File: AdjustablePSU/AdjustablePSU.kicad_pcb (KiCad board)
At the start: 2 copper layers, 99.1 x 96.5 mm, 39 parts

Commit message: RevC update
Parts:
- added HS1: Heatsink, Heatsink:Heatsink_SheetType_50x7mm_2Fixations, F.Cu at (149.4, 59.8)
- C_NEG6, C_POS6: footprint Capacitor_SMD:CP_Elec_6.3x3.9 -> Capacitor_SMD:CP_Elec_10x12.6
- moved D_POS3 3.43 mm to (179.6, 76.7)
- moved D_POS2 3.08 mm to (173.1, 76.8)
- moved D_NEG3 2.30 mm to (116.1, 77.5)
- moved D_POS1 2.21 mm to (165.6, 76.8)
- moved D_NEG2 1.63 mm to (123.3, 77.5)
- moved D_NEG1 0.13 mm to (130.6, 77.5)
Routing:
- net GND: track 90.1 -> 93.9 mm
- net /DC_POS_IN: track 121.1 -> 118.1 mm
- net /AC_IN: track 76.6 -> 74.2 mm
- net /12VDC_POS_REG: track 97.5 -> 99.5 mm
- net /DC_NEG_IN: track 126.8 -> 125.1 mm
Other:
- board text added: "Rev C Chris Sutton 0619"

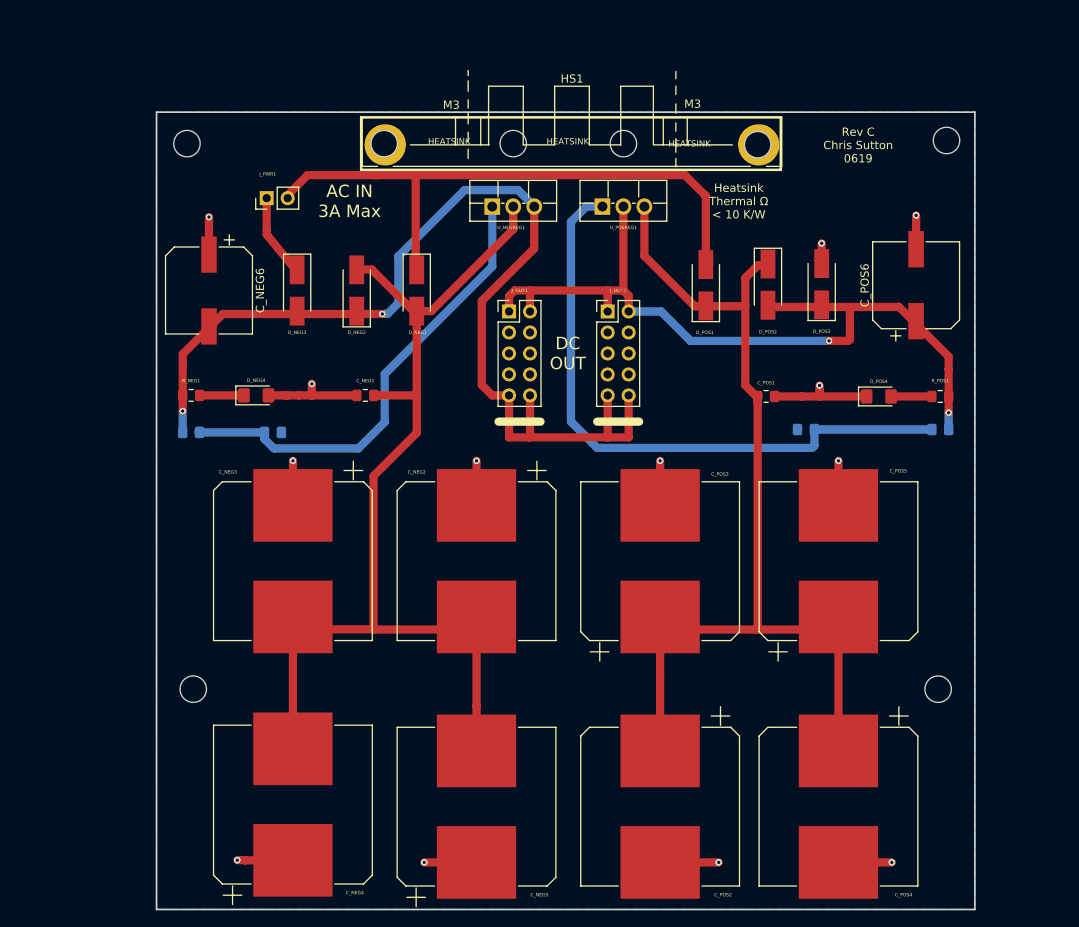
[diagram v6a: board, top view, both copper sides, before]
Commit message: Added hybrid THT/SMT RevD
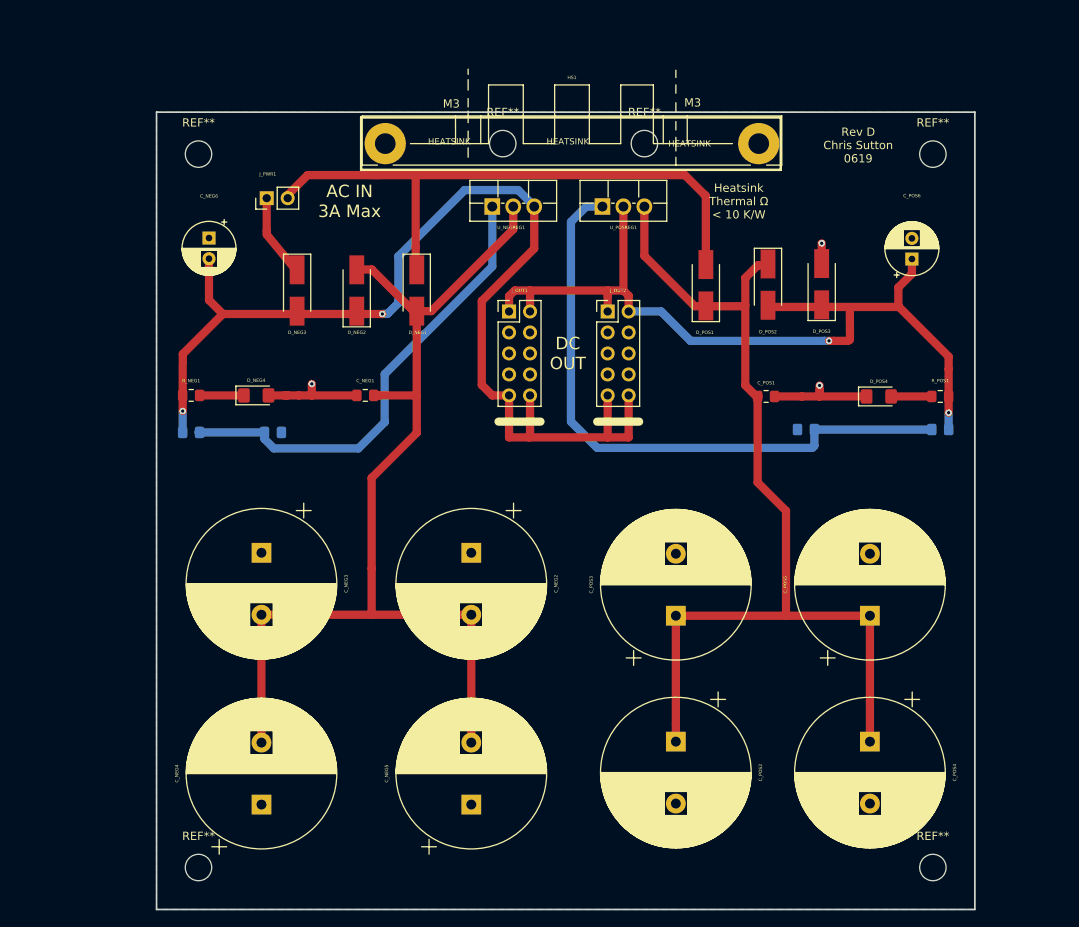
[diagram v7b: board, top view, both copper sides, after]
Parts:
- removed the REF** at (171.8, 59.8)
- removed the REF** at (126.6, 59.7)
- removed the REF** at (102.7, 59.7)
- removed the REF** at (194.7, 59.3)
- removed the REF** at (193.7, 125.7)
- removed the REF** at (103.5, 125.7)
- removed the REF** at (142.2, 59.7)
- removed the REF** at (155.6, 59.7)
- added REF**: MountingHole_3.2mm_M3_DIN965, MountingHole:MountingHole_3.2mm_M3_DIN965, F.Cu at (193.0, 61.0)
- added REF**: MountingHole_3.2mm_M3_DIN965, MountingHole:MountingHole_3.2mm_M3_DIN965, F.Cu at (104.1, 61.0)
- added REF**: MountingHole_3.2mm_M3_DIN965, MountingHole:MountingHole_3.2mm_M3_DIN965, F.Cu at (104.1, 147.3)
- added REF**: MountingHole_3.2mm_M3_DIN965, MountingHole:MountingHole_3.2mm_M3_DIN965, F.Cu at (193.0, 147.3)
- added REF**: MountingHole_3.2mm_M3_DIN965, MountingHole:MountingHole_3.2mm_M3_DIN965, F.Cu at (158.1, 59.7)
- added REF**: MountingHole_3.2mm_M3_DIN965, MountingHole:MountingHole_3.2mm_M3_DIN965, F.Cu at (141.0, 59.7)
- C_NEG2, C_NEG3, C_NEG4, C_NEG5, C_POS2, C_POS3, C_POS4, C_POS5: footprint Capacitor_SMD:CP_Elec_18x22 -> Capacitor_THT:CP_Radial_D18.0mm_P7.50mm
- C_NEG6, C_POS6: footprint Capacitor_SMD:CP_Elec_10x12.6 -> Capacitor_THT:CP_Radial_D6.3mm_P2.50mm
- moved C_POS4 8.75 mm to (185.4, 132.1)
- moved C_POS2 8.10 mm to (161.9, 132.1)
- moved C_POS5 7.62 mm to (185.4, 116.8)
- moved C_POS3 6.87 mm to (161.9, 116.8)
- moved C_NEG6 6.35 mm to (105.4, 71.1)
- moved C_NEG3 3.94 mm to (111.8, 109.2)
- moved C_NEG4 3.81 mm to (111.8, 139.7)
- moved C_POS6 3.22 mm to (190.5, 73.7)
- moved C_NEG2 1.20 mm to (137.2, 109.2)
- moved C_NEG5 0.68 mm to (137.2, 139.7)
- moved HS1 0.15 mm to (149.4, 59.7)
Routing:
- net GND: track 93.9 -> 37.1 mm, vias 13 -> 3
- net /12VDC_NEG_REG: track 127.0 -> 134.4 mm
- net /12VDC_POS_REG: track 99.5 -> 106.0 mm
- net /DC_NEG_IN: track 125.1 -> 128.1 mm
- net /DC_POS_IN: track 118.1 -> 120.9 mm
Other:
- board text added: "Rev D Chris Sutton 0619"
- board text removed: "Rev C Chris Sutton 0619"
